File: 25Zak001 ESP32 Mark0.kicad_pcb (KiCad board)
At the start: 2 copper layers, 1 part, among them U1 ESP32-C3-DevKitM-1

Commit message: Pridano USB C
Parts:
- added H1: MountingHole, MountingHole:MountingHole_3.2mm_M3_ISO14580_Pad_TopBottom, F.Cu at (83.0, 48.0)
- added H2: MountingHole, MountingHole:MountingHole_3.2mm_M3_ISO14580_Pad_TopBottom, F.Cu at (172.0, 48.0)
- added H3: MountingHole, MountingHole:MountingHole_3.2mm_M3_ISO14580_Pad_TopBottom, F.Cu at (82.5, 135.5)
- added H4: MountingHole, MountingHole:MountingHole_3.2mm_M3_ISO14580_Pad_TopBottom, F.Cu at (172.0, 135.5)
- added J1: USB_C_Receptacle_PowerOnly_6P, Connector_USB:USB_C_Receptacle_GCT_USB4135-GF-A_6P_TopMnt_Horizontal, F.Cu at (128.4, 137.4)
- moved U1 15.7 mm to (117.1, 42.5)
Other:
- board outline added: 100 x 100 mm

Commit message: Nova verze
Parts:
- removed U1: ESP32-C3-DevKitM-1, RF_Module:ESP32-C3-DevKitM-1
- added A1: ESP32_NODEMCU, ndoemcu:MODULE_ESP32_NODEMCU, F.Cu at (112.5, 70.0)
- added J2: BME280, Connector_PinSocket_2.54mm:PinSocket_1x04_P2.54mm_Vertical, F.Cu at (162.0, 89.0)
- added J3: eInk display, Connector_PinSocket_2.54mm:PinSocket_1x09_P2.54mm_Horizontal, F.Cu at (173.5, 59.4)
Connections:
- J1 pad S1: unconnected-(J1-SHIELD-PadS1) -> GND

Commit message: Dokonceni, plno chyb, nutno opravit
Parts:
- removed A1: ESP32_NODEMCU, ndoemcu:MODULE_ESP32_NODEMCU
- added J4: Conn_01x08_Pin, Connector_PinHeader_2.54mm:PinHeader_1x08_P2.54mm_Vertical, F.Cu at (82.0, 98.0)
- added J5: Conn_01x06_Pin, Connector_PinHeader_2.54mm:PinHeader_1x06_P2.54mm_Vertical, F.Cu at (173.5, 106.9)
- added NodeMCU-C6-DevkitM1: ~, ndoemcu:ESP32-C6-DevKitM-1, F.Cu at (93.0, 42.4)
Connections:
- J1 pad A9: Net-(J1-VBUS-PadA9) -> GND
- J1 pad B9: Net-(J1-VBUS-PadA9) -> GND
- J2 pad 1: /VCC -> GND
- J3 pad 8: /VCC -> GND
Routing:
- net /GPIO12: track 0.00 -> 108.1 mm, vias 0 -> 2
- net /GPIO13: track 0.00 -> 108.0 mm, vias 0 -> 2
- net /GPIO15: track 0.00 -> 106.0 mm, vias 0 -> 2
- net /GPIO14: track 0.00 -> 97.7 mm, vias 0 -> 2
- net /SDA: track 0.00 -> 87.8 mm, vias 0 -> 2
- net /SCL: track 0.00 -> 84.3 mm, vias 0 -> 2
- net /RST: track 0.00 -> 80.9 mm, vias 0 -> 1
- net /GPIO23: track 0.00 -> 78.0 mm
- net /GPIO22: track 0.00 -> 78.0 mm
- net /BUSY: track 0.00 -> 70.7 mm, vias 0 -> 2
- net /CS: track 0.00 -> 60.4 mm
- net /DIN: track 0.00 -> 60.4 mm
- net /DC: track 0.00 -> 60.4 mm
- net /CLK: track 0.00 -> 60.4 mm
- net /GPIO5: track 0.00 -> 60.2 mm
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- added copper zone on F.Cu, net +5V
- added copper zone on B.Cu, net GND

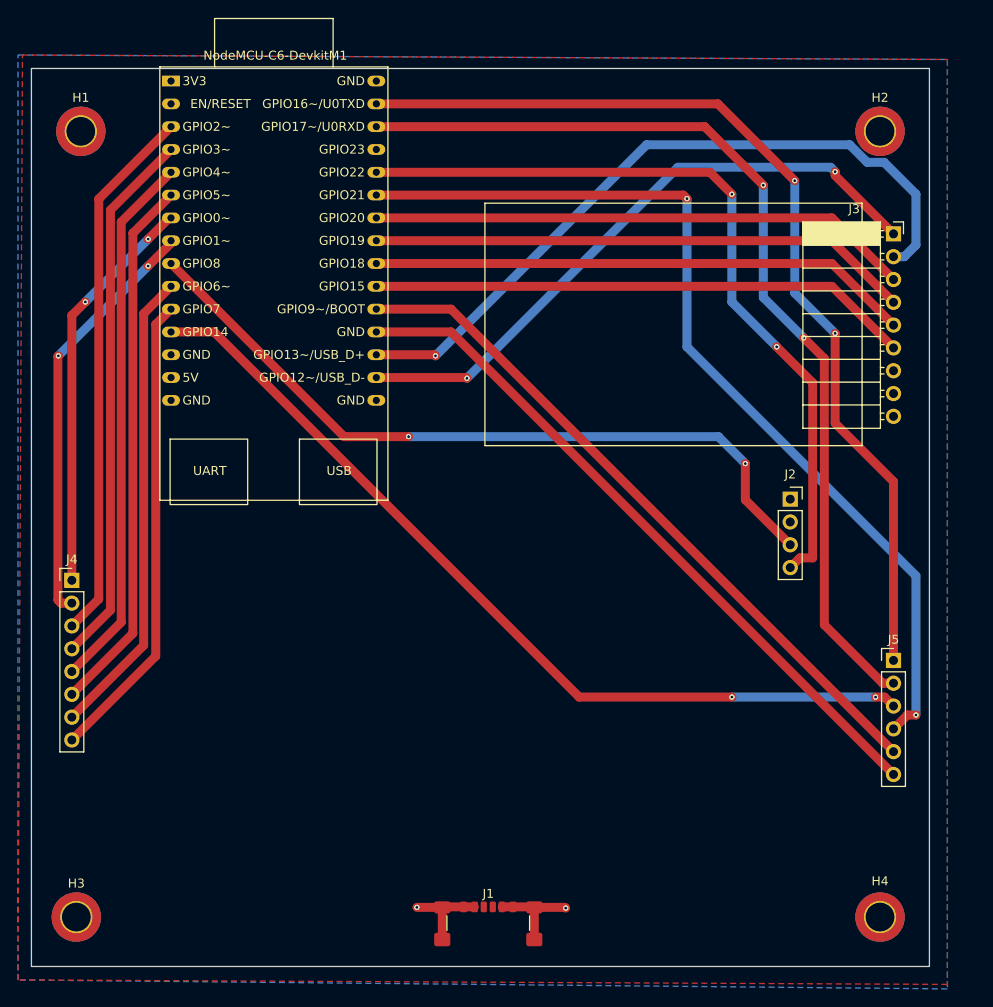
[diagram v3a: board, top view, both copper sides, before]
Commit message: Fairly Big Update
- completly reworked ESP32 devkit
- different sensor
- all unused GPIOs are now available via sockets
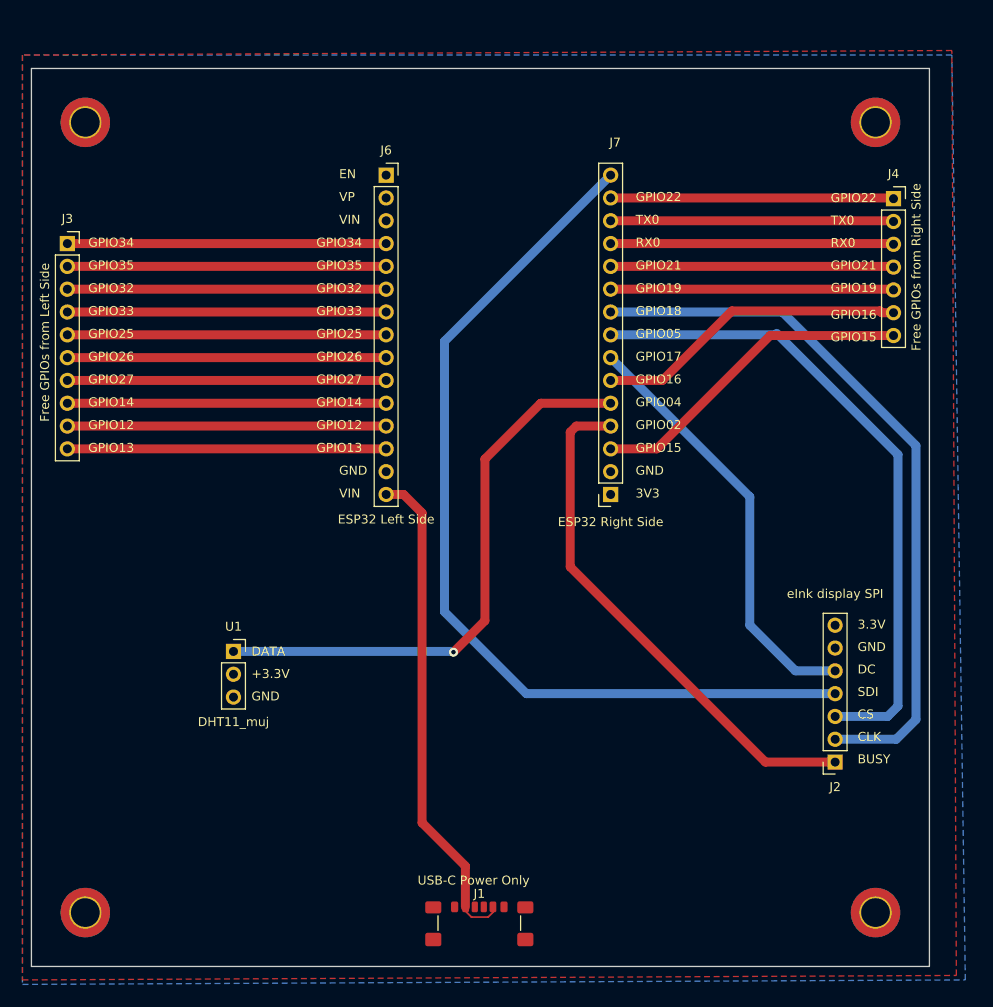
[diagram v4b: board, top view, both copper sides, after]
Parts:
- removed J5: Conn_01x06_Pin, Connector_PinHeader_2.54mm:PinHeader_1x06_P2.54mm_Vertical
- removed NodeMCU-C6-DevkitM1: ~, ndoemcu:ESP32-C6-DevKitM-1
- added J6: ESP32 Left Side, Connector_PinSocket_2.54mm:PinSocket_1x15_P2.54mm_Vertical, F.Cu at (117.0, 52.9)
- added J7: ESP32 Right Side, Connector_PinSocket_2.54mm:PinSocket_1x15_P2.54mm_Vertical, F.Cu at (142.0, 88.4)
- added U1: DHT11_muj, Connector_PinSocket_2.54mm:PinSocket_1x03_P2.54mm_Vertical, F.Cu at (100.0, 105.9)
- J2: value BME280 -> eInk display SPI; footprint Connector_PinSocket_2.54mm:PinSocket_1x04_P2.54mm_Vertical -> Connector_PinSocket_2.54mm:PinSocket_1x07_P2.54mm_Vertical
- J3: value eInk display -> Free GPIOs from Left Side; footprint Connector_PinSocket_2.54mm:PinSocket_1x09_P2.54mm_Horizontal -> Connector_PinSocket_2.54mm:PinSocket_1x10_P2.54mm_Vertical
- J4: value Conn_01x08_Pin -> Free GPIOs from Right Side; footprint Connector_PinHeader_2.54mm:PinHeader_1x08_P2.54mm_Vertical -> Connector_PinSocket_2.54mm:PinSocket_1x07_P2.54mm_Vertical
- moved J4 100.9 mm to (173.5, 55.5)
- moved J3 92.0 mm to (81.5, 60.5)
- moved J2 29.7 mm to (167.0, 118.2), turned to 180 degrees
- moved H1 1.12 mm to (83.5, 47.0)
- moved H2 1.12 mm to (171.5, 47.0)
- moved H3 1.12 mm to (83.5, 135.0)
- moved J1 1.00 mm to (127.4, 137.4)
- moved H4 0.71 mm to (171.5, 135.0)
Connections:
- J1 pad A9: GND -> +5V
- J1 pad B9: GND -> +5V
- J2 pad 1: GND -> /BUSY
- J2 pad 2: GND -> /CLK
- J2 pad 3: /SCL -> /CS
- J2 pad 4: /SDA -> /SDI
- J3 pad 1: /BUSY -> /GPIO34
- J3 pad 2: /RST -> /GPIO35
- J3 pad 3: /DC -> /GPIO32
- J3 pad 4: /CS -> /GPIO33
- J3 pad 5: /CLK -> /GPIO25
- J3 pad 6: /DIN -> /GPIO26
- J3 pad 7: GND -> /GPIO27
- J3 pad 8: GND -> /GPIO14
- J3 pad 9: (no net) -> /GPIO12
- J4 pad 1: /GPIO0 -> /GPIO22
- J4 pad 2: /GPIO1 -> /TX0
- J4 pad 3: /GPIO2 -> /RX0
- J4 pad 4: /GPIO3 -> /GPIO21
- J4 pad 5: /GPIO4 -> /GPIO19
- J4 pad 6: /GPIO5 -> /GPIO16
- J4 pad 7: /GPIO6 -> /GPIO15
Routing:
- net /SDI: track 0.00 -> 103.6 mm
- net /SDA: track 87.8 -> 0.00 mm, vias 2 -> 0
- net /SCL: track 84.3 -> 0.00 mm, vias 2 -> 0
- net /RST: track 80.9 -> 0.00 mm, vias 1 -> 0
- net /GPIO23: track 78.0 -> 0.00 mm
- net /GPIO12: track 108.1 -> 35.5 mm, vias 2 -> 0
- net /GPIO13: track 108.0 -> 35.5 mm, vias 2 -> 0
- net /GPIO15: track 106.0 -> 37.0 mm, vias 2 -> 0
- net /DATA: track 0.00 -> 64.1 mm, vias 0 -> 1
- net /GPIO14: track 97.7 -> 35.5 mm, vias 2 -> 0
- net /DIN: track 60.4 -> 0.00 mm
- net /GPIO5: track 60.2 -> 0.00 mm
- net /GPIO3: track 60.2 -> 0.00 mm
- net /GPIO4: track 60.2 -> 0.00 mm
- net /GPIO2: track 60.2 -> 0.00 mm
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- added copper zone on B.Cu, net +3.3V
- added copper zone on F.Cu, net GND
- removed copper zone on F.Cu, net +5V
- removed copper zone on B.Cu, net GND
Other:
- board text added: "+3.3V"
- board text added: "3.3V"
- board text added: "3V3"
- board text added: "BUSY"
- board text added: "CLK"
- board text added: "CS"
- board text added: "DATA"
- board text added: "DC"
- board text added: "EN"
- board text added: "GND"
- board text added: "GPIO02"
- board text added: "GPIO04"
- board text added: "GPIO05"
- board text added: "GPIO12"
- board text added: "GPIO13"
- board text added: "GPIO14"
- board text added: "GPIO15"
- board text added: "GPIO16"
- board text added: "GPIO17"
- board text added: "GPIO18"
- board text added: "GPIO19"
- board text added: "GPIO21"
- board text added: "GPIO22"
- board text added: "GPIO25"
- board text added: "GPIO26"
- board text added: "GPIO27"
- board text added: "GPIO32"
- board text added: "GPIO33"
- board text added: "GPIO34"
- board text added: "GPIO35"
- board text added: "RX0"
- board text added: "SDI"
- board text added: "TX0"
- board text added: "USB-C Power Only"
- board text added: "VIN"
- board text added: "VP"

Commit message: Rev1 created for PCB
Because Rev0 is virutally unusable in current state.
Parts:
- added QR*****: QR_kod_esp32_mod0, ndoemcu:QR_kod_esp32_mod0, F.Cu at (98.0, 128.0)
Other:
- board text added: "ESP32 Weather Station Mark0 Rev0"
- board text added: "https://github.com/zdenekru/ESP32-Mark0"
